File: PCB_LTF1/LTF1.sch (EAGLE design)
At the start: 18 parts, among them X1 OPAMP, X2 OPAMP

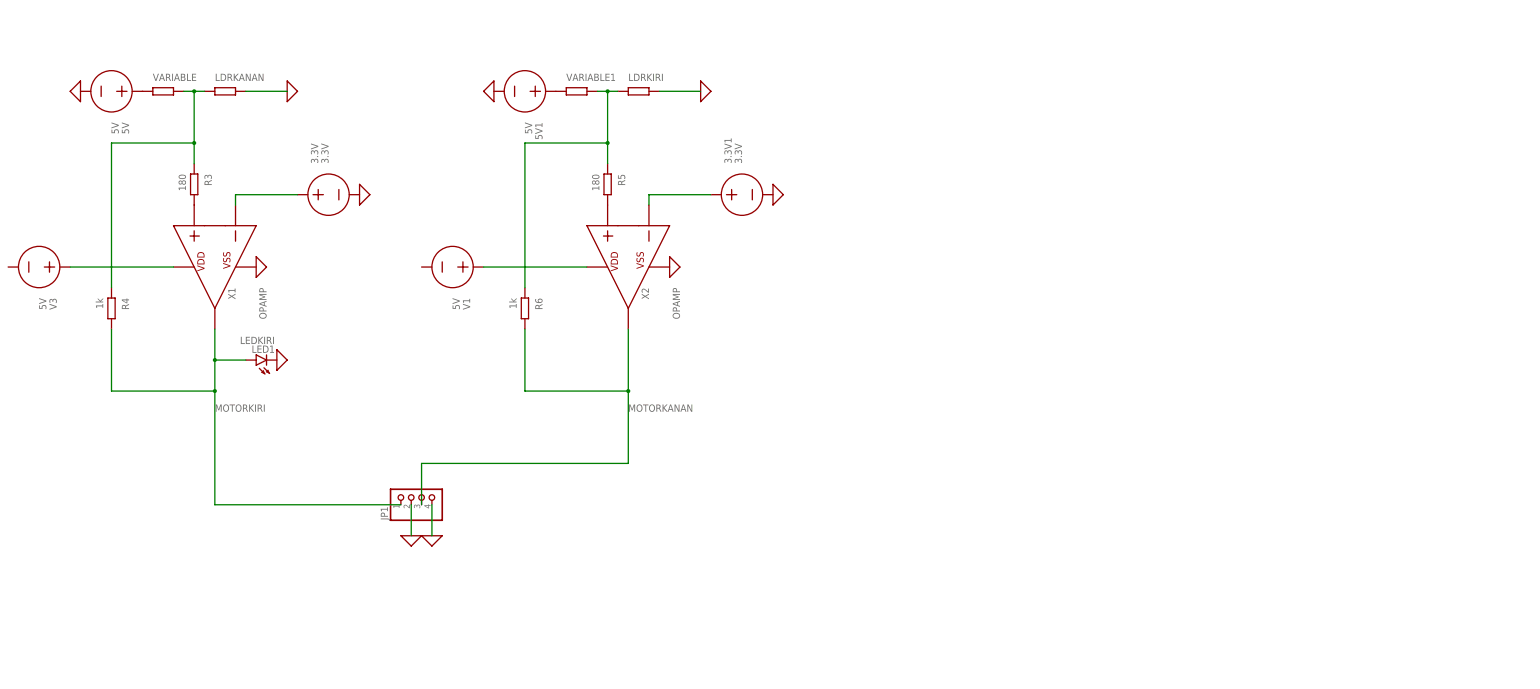
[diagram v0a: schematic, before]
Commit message: op amp belum kesambung
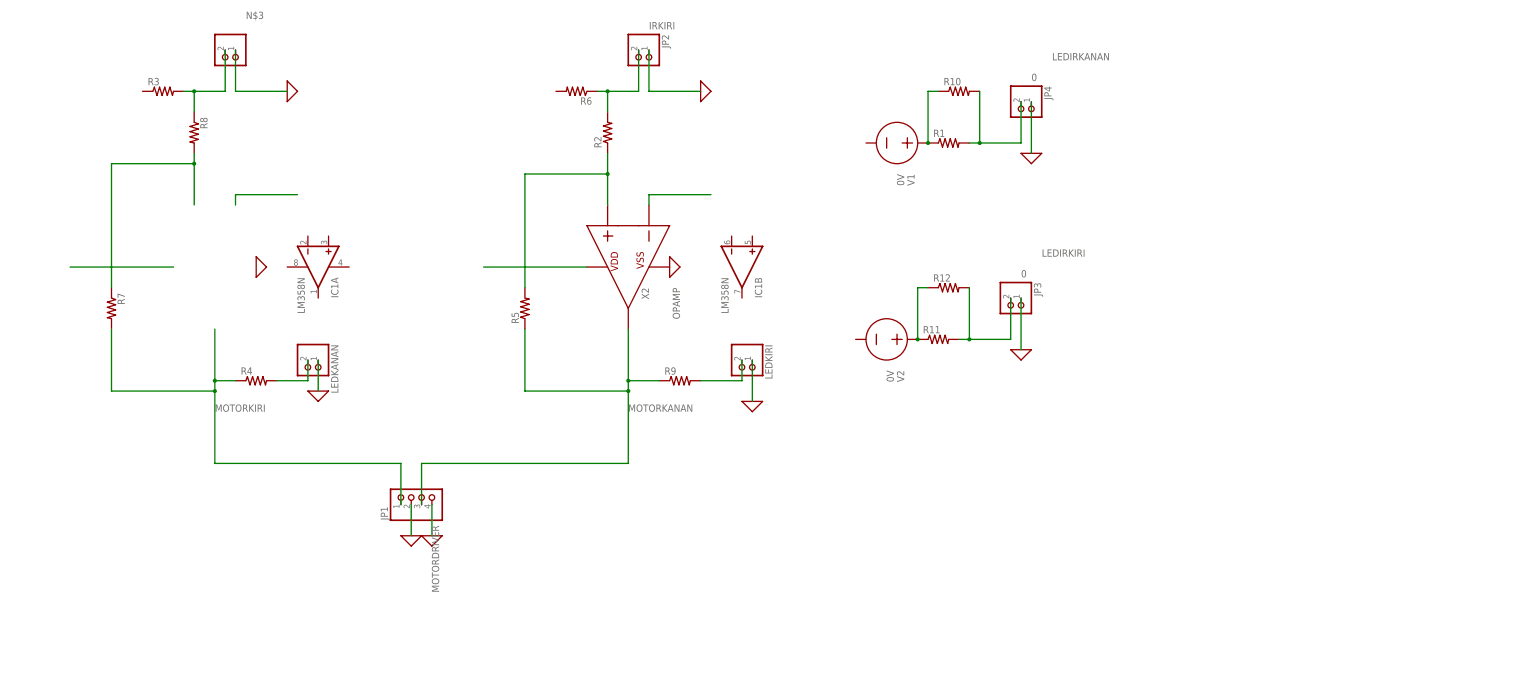
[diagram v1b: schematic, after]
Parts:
- removed 3.3V, 3.3V1: 3.3V, ngspice-simulation:VOLTAGE
- removed 5V, 5V1, V3: 5V, ngspice-simulation:VOLTAGE
- removed LDRKANAN, LDRKIRI, VARIABLE, VARIABLE1: (no value), ngspice-simulation:R
- removed LED1: LEDKIRI, led:LED5MM
- removed X1: OPAMP, ngspice-simulation:OPAMP
- added IC1: LM358N, linear:LM358N
- added IRKANAN, JP2, JP3, JP4, LEDKANAN, LEDKIRI: (no value), pinhead:PINHD-1X2
- added R1, R10, R11, R12, R2, R7, R8, R9: (no value), rcl:R-US_0204/7
- added V2: 0V, ngspice-simulation:VOLTAGE
- R3, R5: value 180 -> (none); device ngspice-simulation:R -> rcl:R-US_0204/7
- R4, R6: value 1k -> (none); device ngspice-simulation:R -> rcl:R-US_0204/7
- V1: value 5V -> 0V
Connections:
- removed net N$4: V3.+, X1.VDD
- removed net N$5: 3.3V.+, X1.N
- removed net N$6: 5V1.+, VARIABLE1.1
- new net IRKANAN: R7.1, R8.2
- new net IRKIRI: JP2.1
- new net LDRKANAN: IRKANAN.1
- new net LEDIRKANAN: JP4.2
- new net LEDIRKIRI: JP3.2
- new net MOTORDRIVER: JP1.2
- new net N$11: LEDKIRI.2, R9.2
- new net N$12: R1.2, R10.2
- new net N$13: R11.2, R12.2
- new net N$14: JP2.2, R2.2, R6.1
- net 0: now also JP3.1, JP4.1, LEDKANAN.1, LEDKIRI.1; no longer 3.3V.-, 3.3V1.-, 5V.-, 5V1.-, JP1.2, LDRKANAN.2, LDRKIRI.2, LED1.C, X1.VSS
- net MOTORKANAN: now also R5.1, R9.1; no longer R6.2
- net MOTORKIRI: now also R4.1, R7.2; no longer LED1.A, R4.2, X1.VOUT
- net N$1: now also R1.1, R10.1, V1.+; no longer 5V.+, VARIABLE.1
- net N$10: no longer 3.3V1.+
- net N$2: now also R11.1, R12.1, V2.+; no longer LDRKANAN.1, R3.1, R4.1, VARIABLE.2
- net N$3: now also IRKANAN.2, R8.1; no longer X1.P
- net N$7: now also R2.1, R5.2, X2.P; no longer LDRKIRI.1, R5.1, R6.1, VARIABLE1.2
- net N$8: now also LEDKANAN.2, R4.2; no longer R5.2, X2.P
- net N$9: no longer V1.+
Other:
- moved on the sheet: V1

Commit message: done sch
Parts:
- removed IRKANAN, LEDKANAN: (no value), pinhead:PINHD-1X2
- removed V1, V2: 0V, ngspice-simulation:VOLTAGE
- added JP5, LEDKIRI1: (no value), pinhead:PINHD-1X2
- added Q1, Q2: BD139, transistor-npn:BD139
- added R13, R14, R15, R16: 1k, rcl:R-US_0204/7
- added X1: (no value), con-wago-500:W237-103
- R1, R10: value (none) -> 1k
- R11, R3, R4, R5: value (none) -> 150k
- R12, R2, R7, R9: value (none) -> 180
- R6, R8: value (none) -> 10k
- X2: value OPAMP -> (none); device ngspice-simulation:OPAMP -> con-wago-500:W237-103
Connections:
- removed net IRKANAN: R7.1, R8.2
- removed net IRKIRI: JP2.1
- removed net LDRKANAN: IRKANAN.1
- removed net LEDIRKIRI: JP3.2
- removed net MOTORKIRI: JP1.1, R4.1, R7.2
- removed net N$1: R1.1, R10.1, V1.+
- removed net N$12: R1.2, R10.2
- removed net N$13: R11.2, R12.2
- removed net N$2: R11.1, R12.1, V2.+
- removed net N$9: X2.VDD
- new net +5V: IC1P.V+, JP2.2, JP3.2, Q1.C, Q2.C, R1.1, R10.1, R13.1, R14.1, R15.1, R16.1, X1-1.KL, X2-1.KL
- new net LEDIRKANAN1: JP5.2, R14.2, R15.2, R16.2
- new net MOTORKANAN1: IC1A.OUT, Q2.B, R11.1, R4.1
- new net N$4: IC1A.+IN, X2-2.KL
- new net N$5: LEDKIRI1.2, R12.2
- new net N$6: JP1.3, Q2.E, R12.1
- net 0: now also IC1P.V-, JP5.1, LEDKIRI1.1, R6.1, R8.1, X1-3.KL, X2-3.KL; no longer JP3.1, LEDKANAN.1, X2.VSS
- net LEDIRKANAN: now also R1.2, R10.2, R13.2
- net MOTORKANAN: now also IC1B.OUT, Q1.B, R3.1; no longer JP1.3, R9.1, X2.VOUT
- net N$10: now also IC1B.+IN, X1-2.KL; no longer X2.N
- net N$14: now also JP2.1, JP3.1, R6.2, R7.2, R8.2; no longer JP2.2, R6.1
- net N$3: now also IC1A.-IN, R11.2, R4.2, R7.1; no longer IRKANAN.2, R3.2, R8.1
- net N$7: now also IC1B.-IN, R3.2; no longer X2.P
- net N$8: now also JP1.1, Q1.E, R9.1; no longer LEDKANAN.2, R4.2
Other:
- moved on the sheet: IC1A, IC1B, JP2, JP3, JP4, R1, R10, R11, R12, R3, R4, R6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

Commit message: done routing and PCB :+1:
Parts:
- removed JP2, JP3, JP4, JP5, LEDKIRI, LEDKIRI1: (no value), pinhead:PINHD-1X2
- removed Q2: BD139, transistor-npn:BD139
- added IRL, IRLEDL, IRLEDR, IRR, LEDL, LEDR, POWER: KF301-2P, KF301-2P:KF301-2P
- added Q4: BD139, transistor-power:BD139
- Q1: device transistor-npn:BD139 -> transistor-power:BD139
- renumbered IC1 to OPAMPKANAN, JP1 to MOTORDRIVER, X1 to RPOT, X2 to LPOT
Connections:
- removed net MOTORDRIVER: MOTORDRIVER.2
- removed net N$11: LEDKIRI.2, R9.2
- removed net N$14: JP2.1, JP3.1, R2.2, R6.2, R7.2, R8.2
- new net IRKIRI: IRL.2, R2.2, R6.2
- new net N$1: LEDR.1, R9.2
- new net N$2: LEDL.1, R12.2
- net +5V: now also IRL.1, IRR.1, POWER.2, Q4.C; no longer JP2.2, JP3.2, Q2.C
- net 0: now also IRLEDL.2, IRLEDR.2, LEDL.2, LEDR.2, MOTORDRIVER.2, POWER.1; no longer JP4.1, JP5.1, LEDKIRI.1, LEDKIRI1.1
- net LEDIRKANAN: now also IRLEDL.1; no longer JP4.2
- net LEDIRKANAN1: now also IRLEDR.1; no longer JP5.2
- net MOTORKANAN: now also Q4.B; no longer Q1.B
- net MOTORKANAN1: now also Q1.B; no longer Q2.B
- net N$5: now also IRR.2, R7.2, R8.2; no longer LEDKIRI1.2, R12.2
- net N$6: now also Q1.E; no longer Q2.E
- net N$8: now also Q4.E; no longer Q1.E
